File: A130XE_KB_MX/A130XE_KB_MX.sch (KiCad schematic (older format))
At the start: 75 parts, among them J1 34 pin RIBBON KEYBOARD CABLE, J2 Conn_01x02_Male, SW1 KS_RESET, SW10 K_5, SW11 K_I, SW12 K_T, SW13 K_G, SW14 K_SPACE, SW15 K_B, SW16 K_K, SW17 KS_SELECT, SW18 K_4, SW19 K_O, SW2 K_6, SW20 K_R, SW21 K_F, SW22 K_M, SW23 K_V, SW24 K_L, SW25 K_3, SW26 K_P, SW27 K_E, SW28 K_D, SW29 KS_START, SW3 K_U, SW30 K_comma, SW31 K_comdot, SW32 K_C, SW33 K_dot, SW34 K_2, SW35 K_minus, SW36 K_W, SW37 K_S, SW38 K_X, SW39 K_plus, SW4 K_Y, SW40 K_1, SW41 K_equal, SW42 K_Q, SW43 K_A, SW44 K_slash, SW45 K_asterisk, SW46 K_Z, SW47 K_ATARI, SW48 K_ESC, SW49 K_RETURN, SW5 K_H, SW50 K_TAB, SW51 K_CAPS, SW52 K_CTRL, SW53 K_LSHIFT, SW54 K_RSHIFT, SW55 K_BRK, SW56 K_DEL, SW57 K_GT, SW58 K_LT, SW59 K_0, SW6 K_N, SW60 K_9, SW61 K_8, SW62 K_7, SW63 K_SPACE_1, SW64 K_SPACE_2, SW65 K_F1, SW66 K_F2, SW67 K_F3, SW68 K_F4, SW7 KS_HELP, SW8 K_J, SW9 KS_OPTION

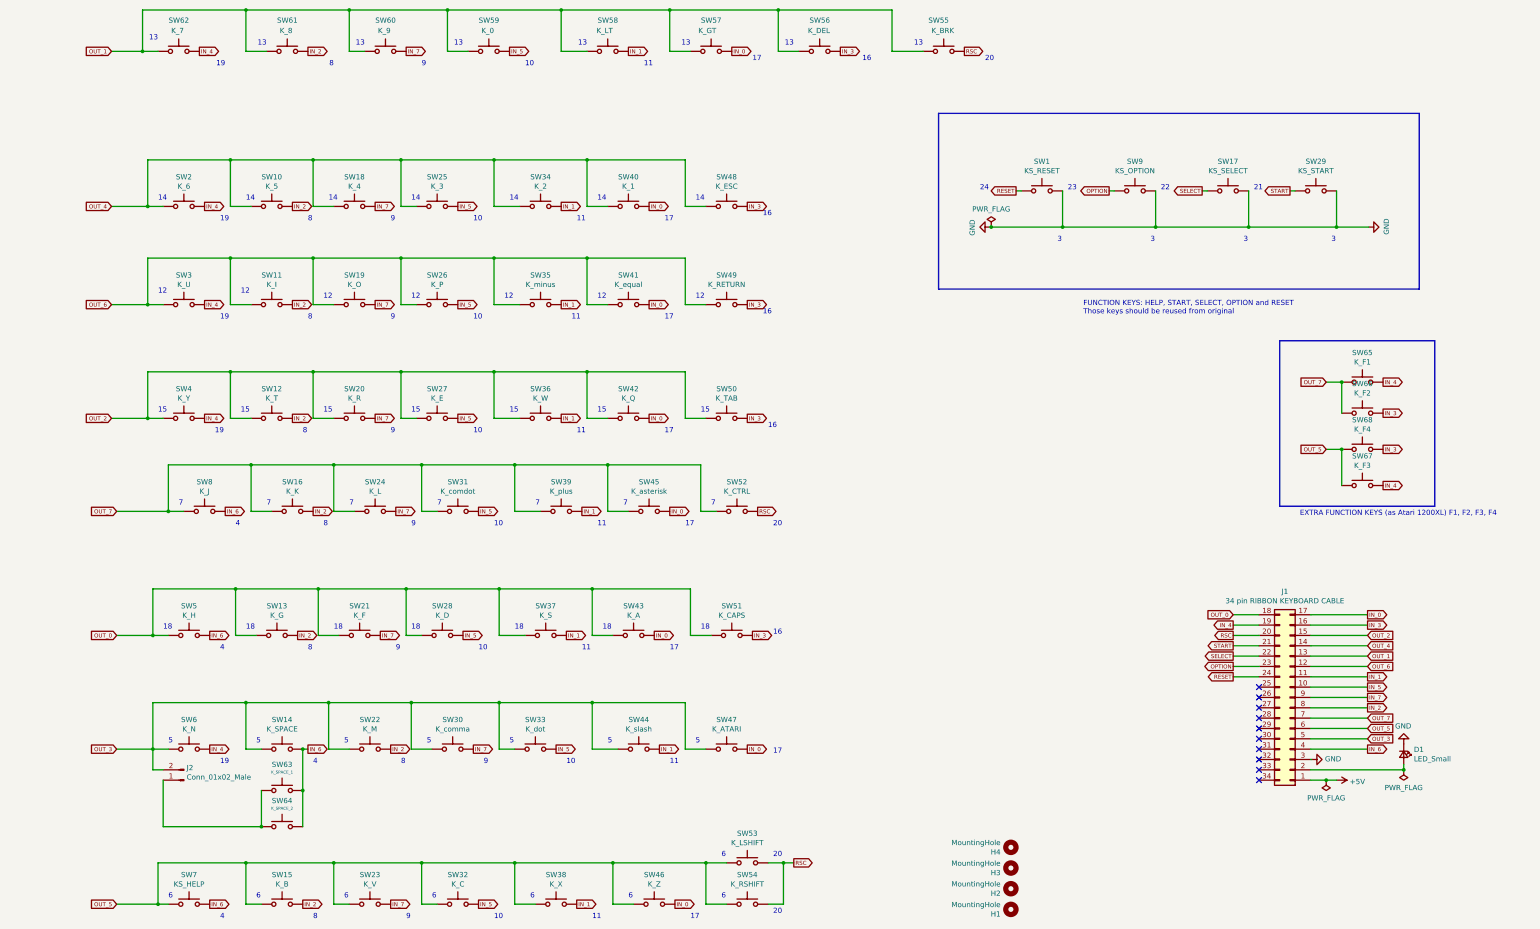
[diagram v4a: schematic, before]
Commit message: Updated with two jumpers for: 1- SHIFT ATARI (single shift) * DEFAULT 1-2 2- USB HID LSHIFT & RSHIFT 2-3
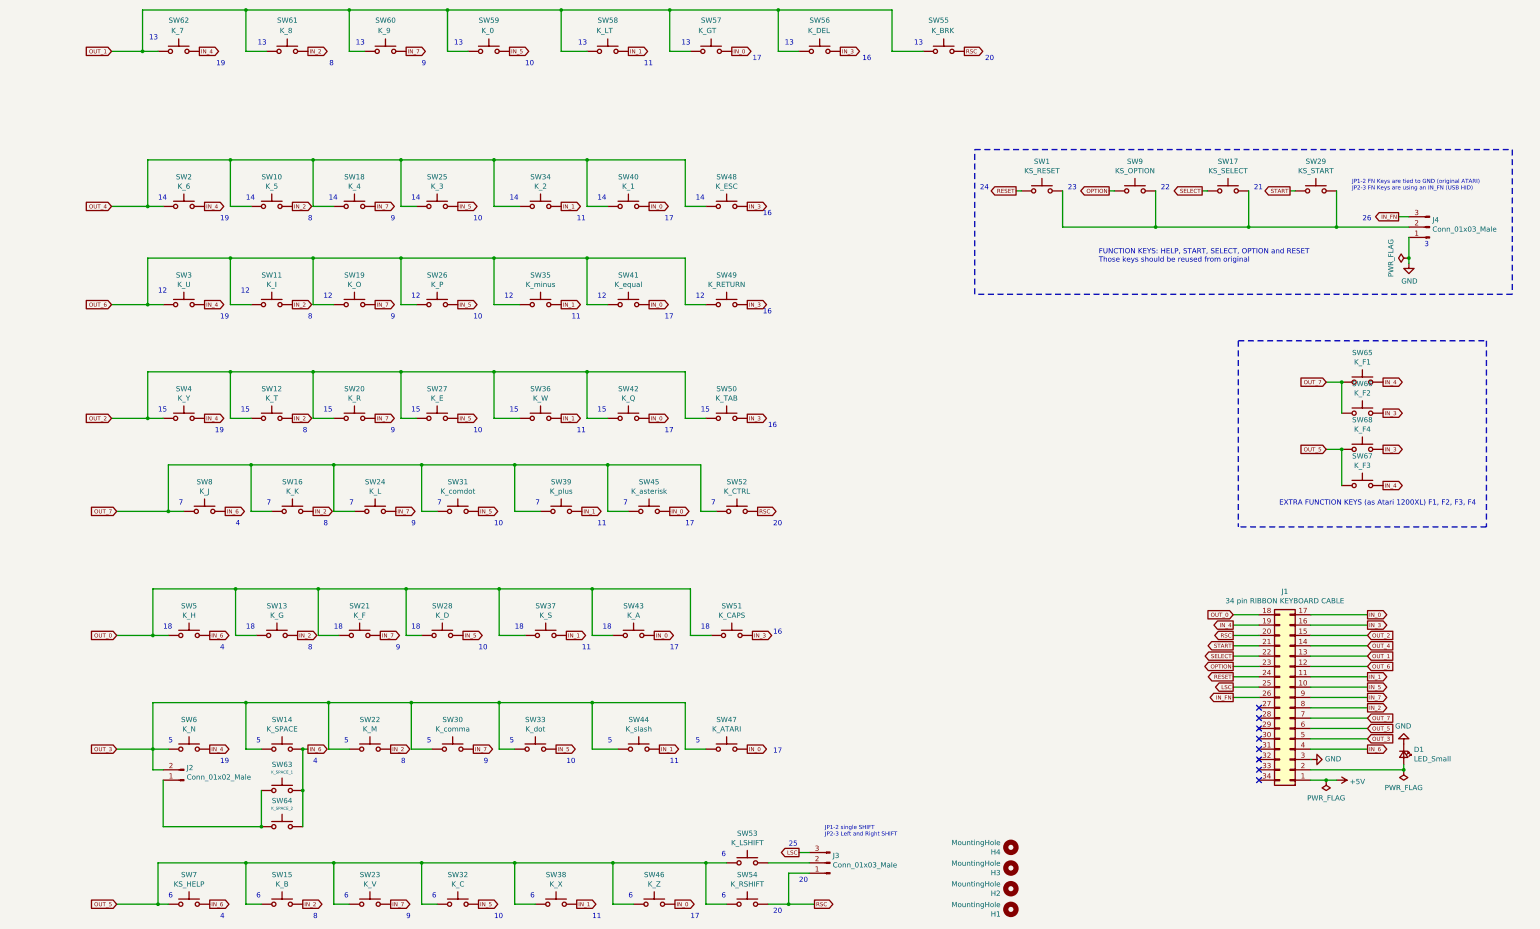
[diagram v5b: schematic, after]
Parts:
- added J3, J4: Conn_01x03_Male, Connector_PinHeader_2.54mm:PinHeader_1x03_P2.54mm_Vertical, symbol Connector:Conn_01x03_Male
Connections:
- net GND: now also J4.1 (Pin_1); no longer SW1.2, SW17.2, SW29.2, SW9.2
- net RSC: now also J3.1 (Pin_1); no longer SW53.2
- net LSC: now reaches J1.25 (Pin_25)
- net LSC: now also J3.3 (Pin_3)
- net IN_FN: now reaches J1.26 (Pin_26)
- net IN_FN: now also J4.3 (Pin_3)
- new net: J4.2 (Pin_2), SW1.2, SW17.2, SW29.2, SW9.2
- new net: J3.2 (Pin_2), SW53.2
- no-connect marks 10 -> 8
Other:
- note added: "25"
- note added: "26"
- note added: "JP1-2 FN Keys are tied to GND (original ATARI)\nJP2-3 FN Keys are using an IN_FN (USB HID)"
- note added: "JP1-2 single SHIFT\nJP2-3 Left and Right SHIFT"
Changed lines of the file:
@@
 Text GLabel 12550 7850 0    39   Output ~ 0
 RESET
-NoConn ~ 12800 7950
-NoConn ~ 12800 8050
 NoConn ~ 12800 8150
 NoConn ~ 12800 8250
@@
 Text GLabel 2650 8550 2    39   Output ~ 0
 IN_4
-Text GLabel 8300 9650 2    39   Output ~ 0
+Text GLabel 8500 10050 2    39   Output ~ 0
 RSC
 Text GLabel 12250 3150 0    39   Output ~ 0
@@
 L power:GND #PWR02
 U 1 1 5F826B7B
-P 13860 3500
-F 0 "#PWR02" H 13860 3250 50  0001 C CNN
-F 1 "GND" H 13865 3327 50  0000 C CNN
-F 2 "" H 13860 3500 50  0001 C CNN
-F 3 "" H 13860 3500 50  0001 C CNN
-	1    13860 3500
-	0    -1   -1   0
-$EndComp
-$Comp
-L power:GND #PWR01
-U 1 1 5F826BB2
-P 10200 3500
-F 0 "#PWR01" H 10200 3250 50  0001 C CNN
-F 1 "GND" H 10205 3327 50  0000 C CNN
-F 2 "" H 10200 3500 50  0001 C CNN
-F 3 "" H 10200 3500 50  0001 C CNN
-	1    10200 3500
-	0    1    1    0
+P 14250 3850
+F 0 "#PWR02" H 14250 3600 50  0001 C CNN
+F 1 "GND" H 14255 3677 50  0000 C CNN
+F 2 "" H 14250 3850 50  0001 C CNN
+F 3 "" H 14250 3850 50  0001 C CNN
+	1    14250 3850
+	1    0    0    -1
 $EndComp
 $Comp
@@
 Wire Wire Line
 	10900 3150 10900 3500
-Connection ~ 10900 3500
 Wire Wire Line
 	10900 3500 11800 3500
@@
 Wire Wire Line
 	13150 3150 13100 3150
-Text Notes 10850 3650 0    50   ~ 0
-3
-Text Notes 11750 3650 0    50   ~ 0
-3
-Text Notes 12650 3650 0    50   ~ 0
-3
-Text Notes 13500 3650 0    50   ~ 0
-3
 Text Notes 10100 3150 0    50   ~ 0
 24
@@
 	1    0    0    -1
 $EndComp
-Wire Wire Line
-	8050 10050 8200 10050
 $Comp
 L Switch:SW_Push SW6
@@
 	7450 9650 7650 9650
 Connection ~ 7450 9650
-Wire Wire Line
-	8050 9650 8200 9650
-Wire Wire Line
-	8200 9650 8200 10050
-Wire Wire Line
-	8200 9650 8300 9650
-Connection ~ 8200 9650
 Text GLabel 1700 1800 0    39   Input ~ 0
 OUT_1
@@
 Wire Wire Line
 	14200 8750 14200 8700
-Wire Wire Line
-	10200 3500 10210 3500
 Text Notes 2250 10000 0    50   ~ 0
 6
@@
 Text Notes 8100 10150 0    50   ~ 0
 20
-Text Notes 8100 9600 0    50   ~ 0
+Text Notes 8350 9850 0    50   ~ 0
 20
 Text Notes 7600 9600 0    50   ~ 0
@@
 Text GLabel 14000 5000 2    39   Output ~ 0
 IN_4
-Wire Bus Line
-	13000 4600 14500 4600
-Wire Bus Line
-	14500 4600 14500 6200
-Wire Bus Line
-	14500 6200 13000 6200
-Wire Bus Line
-	13000 6200 13000 4600
-Text Notes 15100 6300 2    50   ~ 0
+Text Notes 14900 6200 2    50   ~ 0
 EXTRA FUNCTION KEYS (as Atari 1200XL) F1, F2, F3, F4
 $Comp
@@
 	9250 1800 9550 1800
 Connection ~ 8150 1400
-Wire Bus Line
-	9700 2400 14350 2400
-Wire Bus Line
-	14350 2400 14350 4100
-Wire Bus Line
-	14350 4100 9700 4100
-Wire Bus Line
-	9700 4100 9700 2400
-Text Notes 11100 4350 0    50   ~ 0
+Text Notes 11250 3850 0    50   ~ 0
 FUNCTION KEYS: HELP, START, SELECT, OPTION and RESET\nThose keys should be reused from original
-Wire Wire Line
-	13550 3500 13860 3500
 Wire Wire Line
 	13300 8650 13310 8650
@@
 L power:PWR_FLAG #FLG0101
 U 1 1 6020DE80
-P 10210 3500
-F 0 "#FLG0101" H 10210 3575 50  0001 C CNN
-F 1 "PWR_FLAG" H 10210 3674 50  0000 C CNN
-F 2 "" H 10210 3500 50  0001 C CNN
-F 3 "~" H 10210 3500 50  0001 C CNN
-	1    10210 3500
-	1    0    0    -1
-$EndComp
-Connection ~ 10210 3500
-Wire Wire Line
-	10210 3500 10900 3500
+P 14250 3800
+F 0 "#FLG0101" H 14250 3875 50  0001 C CNN
+F 1 "PWR_FLAG" H 14250 3974 50  0000 C CNN
+F 2 "" H 14250 3800 50  0001 C CNN
+F 3 "~" H 14250 3800 50  0001 C CNN
+	1    14250 3800
+	0    -1   -1   0
+$EndComp
+Text GLabel 8350 9550 0    39   Output ~ 0
+LSC
+Wire Wire Line
+	8050 10050 8250 10050
+$Comp
+L Connector:Conn_01x03_Male J3
+U 1 1 601A45B3
+P 8650 9650
+F 0 "J3" H 8623 9580 50  0000 R CNN
+F 1 "Conn_01x03_Male" H 8623 9671 50  0000 R CNN
+F 2 "Connector_PinHeader_2.54mm:PinHeader_1x03_P2.54mm_Vertical" H 8650 9650 50  0001 C CNN
+F 3 "~" H 8650 9650 50  0001 C CNN
+	1    8650 9650
+	-1   0    0    1
+$EndComp
+Wire Wire Line
+	8050 9650 8450 9650
+Wire Wire Line
+	8450 9750 8250 9750
+Wire Wire Line
+	8250 9750 8250 10050
+Connection ~ 8250 10050
+Wire Wire Line
+	8250 10050 8500 10050
+Wire Wire Line
+	8350 9550 8450 9550
+Text Notes 8600 9400 0    39   ~ 0
+JP1-2 single SHIFT\nJP2-3 Left and Right SHIFT
+Text GLabel 12550 7950 0    39   Output ~ 0
+LSC
+Wire Wire Line
+	12800 7950 12550 7950
+$Comp
+L Connector:Conn_01x03_Male J4
+U 1 1 602333E0
+P 14450 3500
+F 0 "J4" H 14423 3430 50  0000 R CNN
+F 1 "Conn_01x03_Male" H 14423 3521 50  0000 R CNN
+F 2 "Connector_PinHeader_2.54mm:PinHeader_1x03_P2.54mm_Vertical" H 14450 3500 50  0001 C CNN
+F 3 "~" H 14450 3500 50  0001 C CNN
+	1    14450 3500
+	-1   0    0    1
+$EndComp
+Wire Wire Line
+	13550 3500 14250 3500
+Wire Wire Line
+	14250 3600 14250 3800
+Wire Wire Line
+	14250 3800 14250 3850
+Connection ~ 14250 3800
+Text Notes 14400 3700 0    50   ~ 0
+3
+Text GLabel 14150 3400 0    39   Output ~ 0
+IN_FN
+Wire Wire Line
+	14150 3400 14250 3400
+Text Notes 13700 3150 0    39   ~ 0
+JP1-2 FN Keys are tied to GND (original ATARI)\nJP2-3 FN Keys are using an IN_FN (USB HID)
+Wire Notes Line
+	15250 2750 15250 4150
+Wire Notes Line
+	15250 4150 10050 4150
+Wire Notes Line
+	10050 4150 10050 2750
+Wire Notes Line
+	10050 2750 15250 2750
+Wire Notes Line
+	12600 4600 15000 4600
+Wire Notes Line
+	15000 4600 15000 6400
+Wire Notes Line
+	15000 6400 12600 6400
+Wire Notes Line
+	12600 4600 12600 6400
+Text GLabel 12550 8050 0    39   Output ~ 0
+IN_FN
+Wire Wire Line
+	12550 8050 12800 8050
+Text Notes 13800 3450 0    50   ~ 0
+26
+Text Notes 8250 9500 0    50   ~ 0
+25
 $EndSCHEMATC

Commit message: Added some text into schematics. Renamed IN_FN as OUT_FN as it is an OUTPUT from microprocessor point of view.
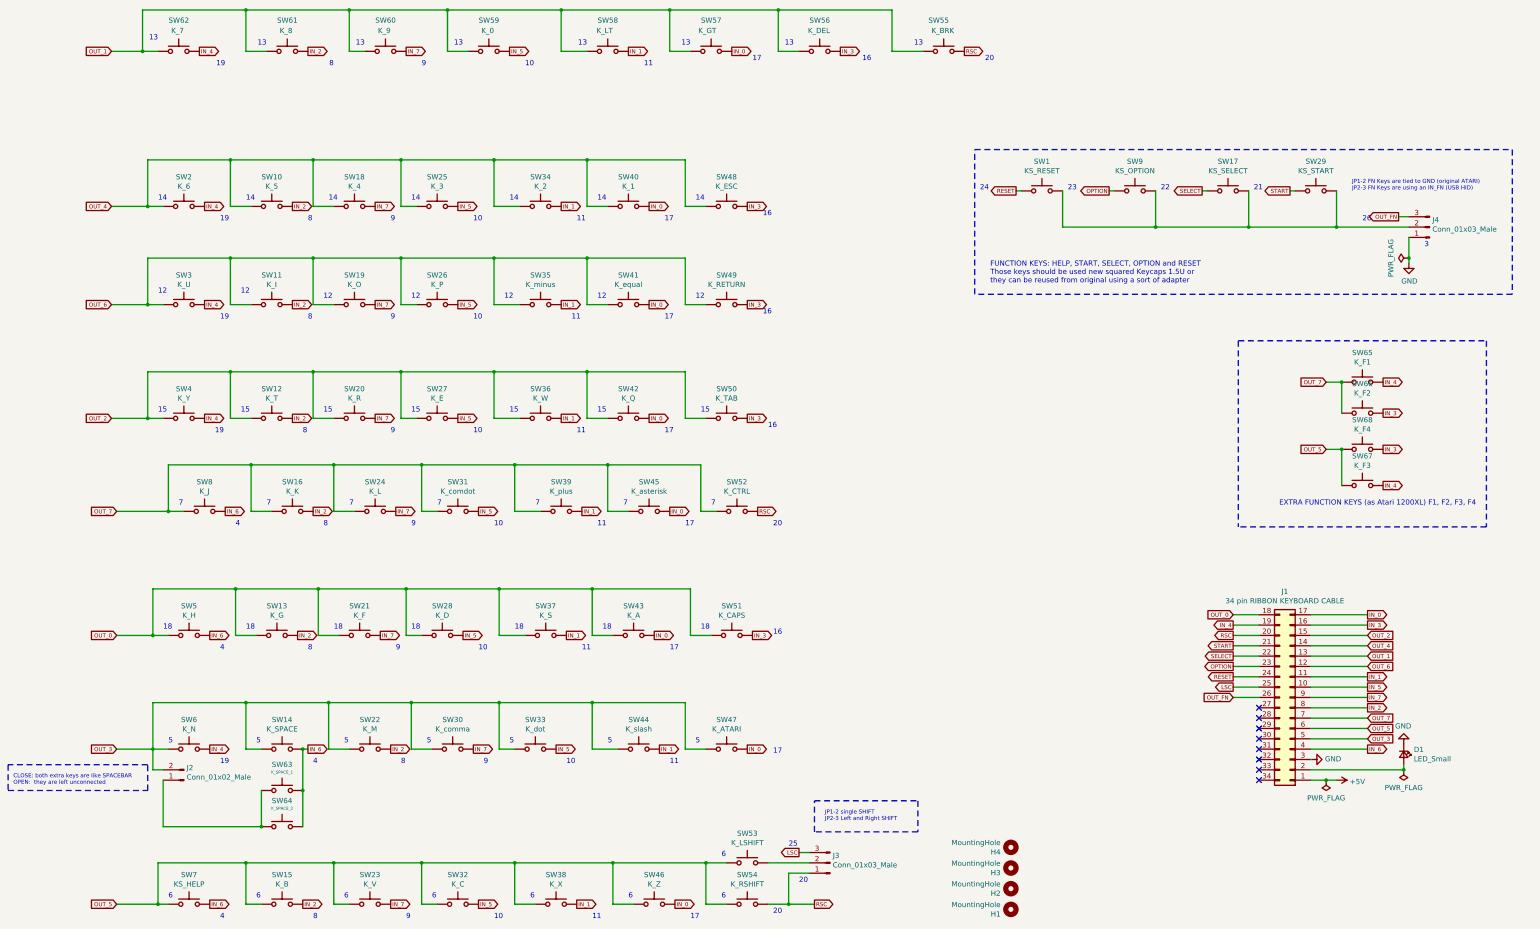
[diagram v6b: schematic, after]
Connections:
- net IN_FN renamed OUT_FN
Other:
- note added: "CLOSE: both extra keys are like SPACEBAR\nOPEN: they are left unconnected"
- note added: "FUNCTION KEYS: HELP, START, SELECT, OPTION and RESET\nThose keys should be used new squared Keycaps 1.5U or\nthey can be reused from original using a sort of adapter"
- note removed: "FUNCTION KEYS: HELP, START, SELECT, OPTION and RESET\nThose keys should be reused from original"
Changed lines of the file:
@@
 	9250 1800 9550 1800
 Connection ~ 8150 1400
-Text Notes 11250 3850 0    50   ~ 0
-FUNCTION KEYS: HELP, START, SELECT, OPTION and RESET\nThose keys should be reused from original
+Text Notes 10200 4050 0    50   ~ 0
+FUNCTION KEYS: HELP, START, SELECT, OPTION and RESET\nThose keys should be used new squared Keycaps 1.5U or\nthey can be reused from original using a sort of adapter
 Wire Wire Line
 	13300 8650 13310 8650
@@
 Wire Wire Line
 	8350 9550 8450 9550
-Text Notes 8600 9400 0    39   ~ 0
+Text Notes 8600 9250 0    39   ~ 0
 JP1-2 single SHIFT\nJP2-3 Left and Right SHIFT
 Text GLabel 12550 7950 0    39   Output ~ 0
@@
 3
 Text GLabel 14150 3400 0    39   Output ~ 0
-IN_FN
+OUT_FN
 Wire Wire Line
 	14150 3400 14250 3400
@@
 Wire Notes Line
 	12600 4600 12600 6400
-Text GLabel 12550 8050 0    39   Output ~ 0
-IN_FN
+Text GLabel 12550 8050 0    39   Input ~ 0
+OUT_FN
 Wire Wire Line
 	12550 8050 12800 8050
@@
 Text Notes 8250 9500 0    50   ~ 0
 25
+Text Notes 750  8900 0    39   ~ 0
+CLOSE: both extra keys are like SPACEBAR\nOPEN:  they are left unconnected
+Wire Notes Line
+	700  8700 700  8950
+Wire Notes Line
+	700  8950 2050 8950
+Wire Notes Line
+	2050 8950 2050 8700
+Wire Notes Line
+	2050 8700 700  8700
+Wire Notes Line
+	8500 9050 9500 9050
+Wire Notes Line
+	9500 9050 9500 9350
+Wire Notes Line
+	9500 9350 8500 9350
+Wire Notes Line
+	8500 9350 8500 9050
 $EndSCHEMATC
